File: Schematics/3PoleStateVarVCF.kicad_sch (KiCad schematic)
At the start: 59 parts, among them J1 Conn_01x12, J2 Conn_01x04, J3 Conn_01x06, J4 Conn_01x03, U1 TL074, U2 SSI2164, U3 TL074, U4 TL074

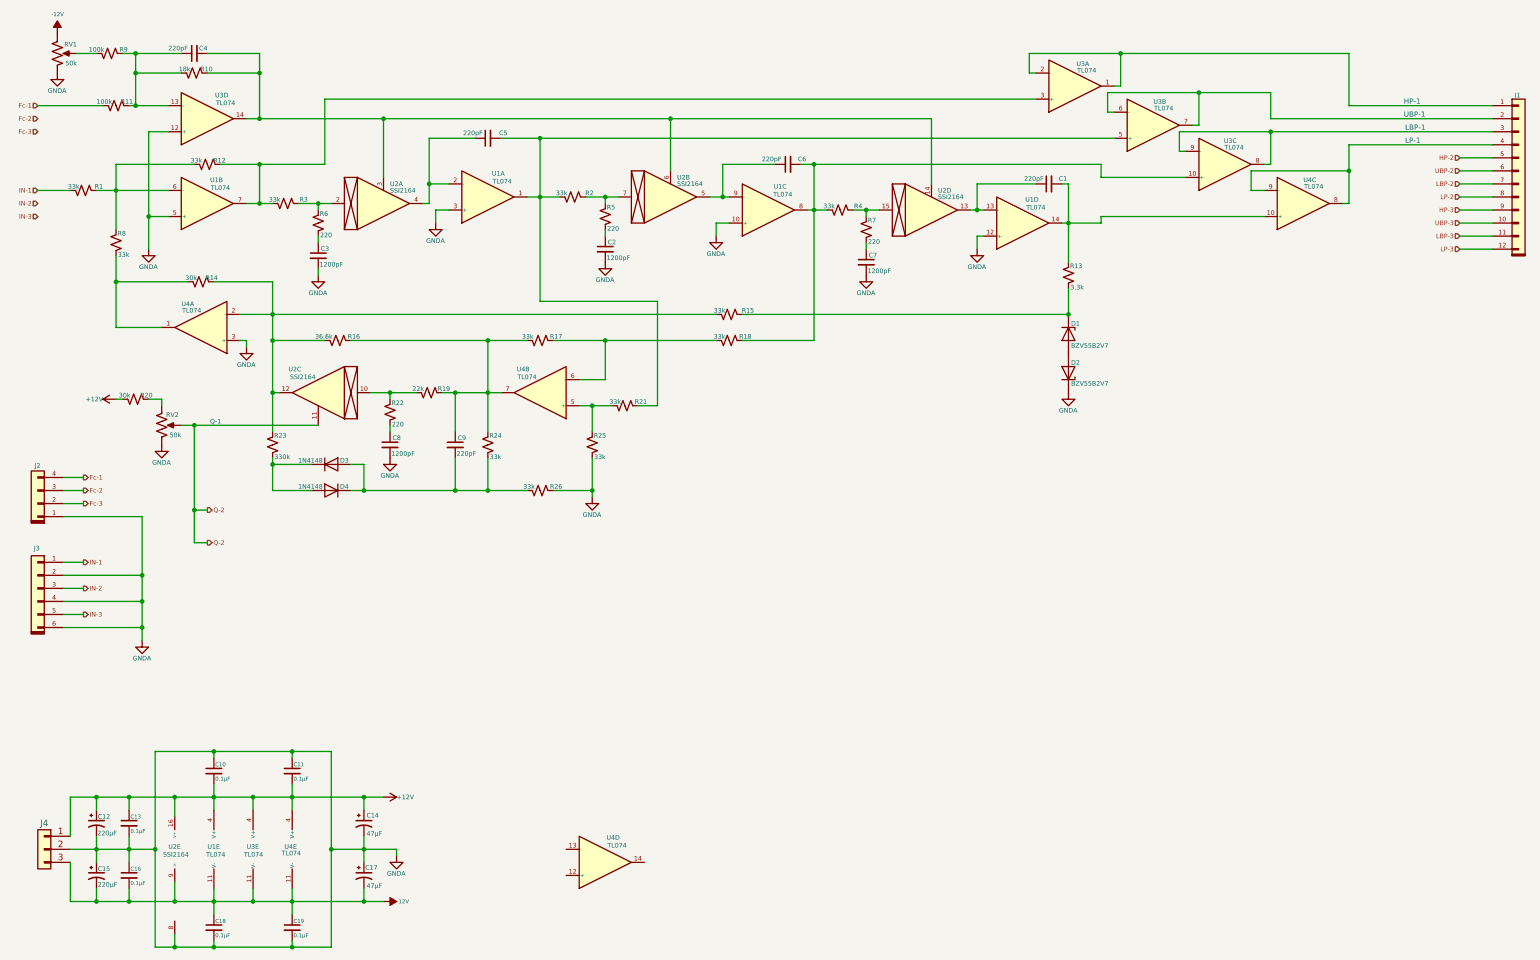
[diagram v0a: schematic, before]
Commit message: Upgreade byte value interface to short.  First stage of refactoring midi input for rotory encoders.  Still needs scaling.
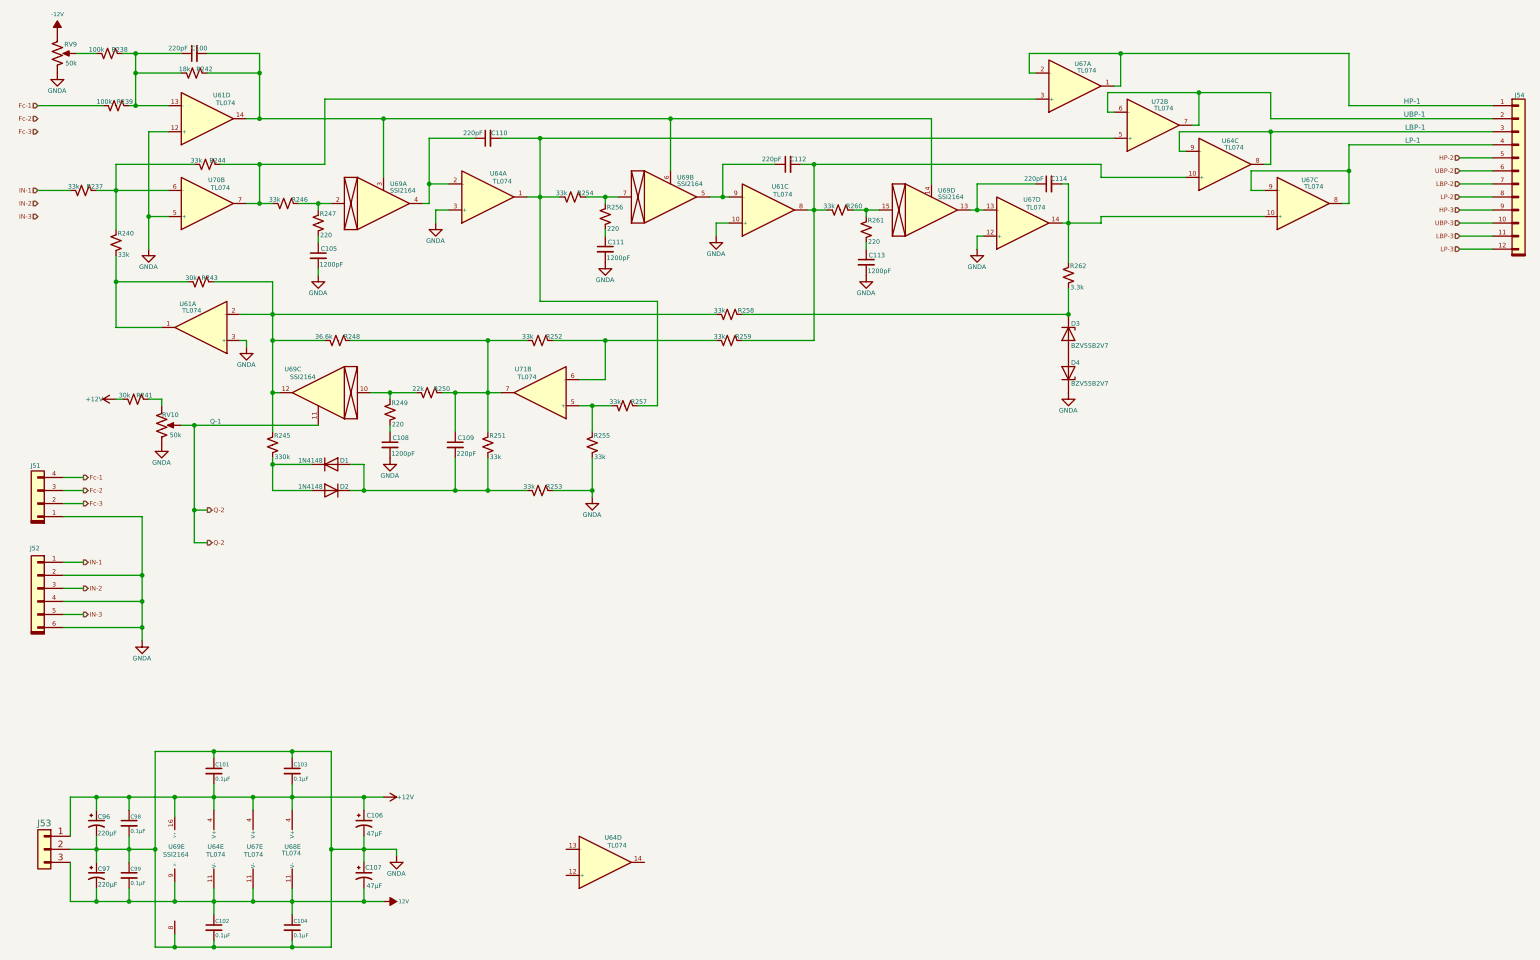
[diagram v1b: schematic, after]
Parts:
- renumbered C4 to C100, C10 to C101, C18 to C102, C11 to C103, C19 to C104, C3 to C105, C14 to C106, C17 to C107, C8 to C108, C9 to C109, C5 to C110, C2 to C111, C6 to C112, C7 to C113, C1 to C114, C12 to C96, C15 to C97, C13 to C98, C16 to C99, D3 to D1, D4 to D2, D1 to D3, D2 to D4, J2 to J51, J3 to J52, J4 to J53, J1 to J54, R1 to R237, R9 to R238, R11 to R239, R8 to R240, R20 to R241, R10 to R242, R14 to R243, R12 to R244, R23 to R245, R3 to R246, R6 to R247, R16 to R248, R22 to R249, R19 to R250, R24 to R251, R17 to R252, R26 to R253, R2 to R254, R25 to R255, R5 to R256, R21 to R257, R15 to R258, R18 to R259, R4 to R260, R7 to R261, R13 to R262, RV2 to RV10, RV1 to RV9, U3 to U61, U1 to U61, U4 to U61, U1 to U64, U4 to U64, U3 to U64, U1 to U67, U3 to U67, U4 to U67, U4 to U68, U2 to U69, U1 to U70, U4 to U71, U3 to U72

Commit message: Updated schematics including VCO and VCF daughter boards
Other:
- title: (none) -> Three State VCF
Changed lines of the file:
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@@
 	(generator_version "8.0")
 	(paper "USLegal")
+	(title_block
+		(title "Three State VCF")
+		(date "2025-01-16")
+		(rev "2.0")
+		(comment 1 "In Development ")
+	)
 	(junction
 		(at 92.71 88.9)

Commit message: Cleaned up page advance on display controls.
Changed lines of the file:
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@@
 (kicad_sch
-	(version 20231120)
+	(version 20250114)
 	(generator "eeschema")
-	(generator_version "8.0")
+	(generator_version "9.0")
 	(paper "USLegal")
 	(title_block
@@
 		(comment 1 "In Development ")
 	)
+	(text "LP-1"
+		(exclude_from_sim no)
+		(at 290.322 40.64 0)
+		(effects
+			(font
+				(size 1.016 1.016)
+			)
+			(justify left bottom)
+		)
+	)
+	(text "UBP-1"
+		(exclude_from_sim no)
+		(at 290.068 35.56 0)
+		(effects
+			(font
+				(size 1.016 1.016)
+			)
+			(justify left bottom)
+		)
+	)
+	(text "LBP-1"
+		(exclude_from_sim no)
+		(at 290.322 38.1 0)
+		(effects
+			(font
+				(size 1.016 1.016)
+			)
+			(justify left bottom)
+		)
+	)
+	(text "HP-1"
+		(exclude_from_sim no)
+		(at 290.068 33.02 0)
+		(effects
+			(font
+				(size 1.016 1.016)
+			)
+			(justify left bottom)
+		)
+	)
+	(text "Q-1"
+		(exclude_from_sim no)
+		(at 57.658 95.25 0)
+		(effects
+			(font
+				(size 0.889 0.889)
+			)
+			(justify left bottom)
+		)
+	)
 	(junction
 		(at 92.71 88.9)
@@
 		)
 	)
-	(text "LP-1"
-		(exclude_from_sim no)
-		(at 290.322 40.64 0)
-		(effects
-			(font
-				(size 1.016 1.016)
-			)
-			(justify left bottom)
-		)
-	)
-	(text "UBP-1"
-		(exclude_from_sim no)
-		(at 290.068 35.56 0)
-		(effects
-			(font
-				(size 1.016 1.016)
-			)
-			(justify left bottom)
-		)
-	)
-	(text "LBP-1"
-		(exclude_from_sim no)
-		(at 290.322 38.1 0)
-		(effects
-			(font
-				(size 1.016 1.016)
-			)
-			(justify left bottom)
-		)
-	)
-	(text "HP-1"
-		(exclude_from_sim no)
-		(at 290.068 33.02 0)
-		(effects
-			(font
-				(size 1.016 1.016)
-			)
-			(justify left bottom)
-		)
-	)
-	(text "Q-1"
-		(exclude_from_sim no)
-		(at 57.658 95.25 0)
-		(effects
-			(font
-				(size 0.889 0.889)
-			)
-			(justify left bottom)
-		)
-	)
 	(hierarchical_label "HP-3"
 		(shape input)
 		(at 300.99 53.34 180)
-		(fields_autoplaced yes)
 		(effects
 			(font
@@
 		(shape output)
 		(at 33.02 105.41 0)
-		(fields_autoplaced yes)
 		(effects
 			(font
@@
 		(shape output)
 		(at 33.02 127 0)
-		(fields_autoplaced yes)
 		(effects
 			(font
@@
 		(shape input)
 		(at 24.13 35.56 180)
-		(fields_autoplaced yes)
 		(effects
 			(font
@@
 		(shape input)
 		(at 24.13 33.02 180)
-		(fields_autoplaced yes)
 		(effects
 			(font
@@
 		(shape input)
 		(at 300.99 58.42 180)
-		(fields_autoplaced yes)
 		(effects
 			(font
@@
 		(shape output)
 		(at 33.02 121.92 0)
-		(fields_autoplaced yes)
 		(effects
 			(font
@@
 		(shape input)
 		(at 24.13 54.61 180)
-		(fields_autoplaced yes)
 		(effects
 			(font
@@
 		(shape input)
 		(at 300.99 43.18 180)
-		(fields_autoplaced yes)
 		(effects
 			(font
@@
 		(shape output)
 		(at 33.02 107.95 0)
-		(fields_autoplaced yes)
 		(effects
 			(font
@@
 		(shape input)
 		(at 24.13 49.53 180)
-		(fields_autoplaced yes)
 		(effects
 			(font
@@
 		(shape input)
 		(at 300.99 50.8 180)
-		(fields_autoplaced yes)
 		(effects
 			(font
@@
 		(shape input)
 		(at 300.99 55.88 180)
-		(fields_autoplaced yes)
 		(effects
 			(font
@@
 		(shape output)
 		(at 33.02 110.49 0)
-		(fields_autoplaced yes)
 		(effects
 			(font
@@
 		(shape output)
 		(at 57.15 118.11 0)
-		(fields_autoplaced yes)
 		(effects
 			(font
@@
 		(shape input)
 		(at 300.99 45.72 180)
-		(fields_autoplaced yes)
 		(effects
 			(font
@@
 		(shape input)
 		(at 24.13 38.1 180)
-		(fields_autoplaced yes)
 		(effects
 			(font
@@
 		(shape output)
 		(at 57.15 111.76 0)
-		(fields_autoplaced yes)
 		(effects
 			(font
@@
 		(shape input)
 		(at 24.13 52.07 180)
-		(fields_autoplaced yes)
 		(effects
 			(font
@@
 		(shape input)
 		(at 300.99 48.26 180)
-		(fields_autoplaced yes)
 		(effects
 			(font
@@
 		(shape input)
 		(at 300.99 60.96 180)
-		(fields_autoplaced yes)
 		(effects
 			(font
@@
 		(shape output)
 		(at 33.02 132.08 0)
-		(fields_autoplaced yes)
 		(effects
 			(font

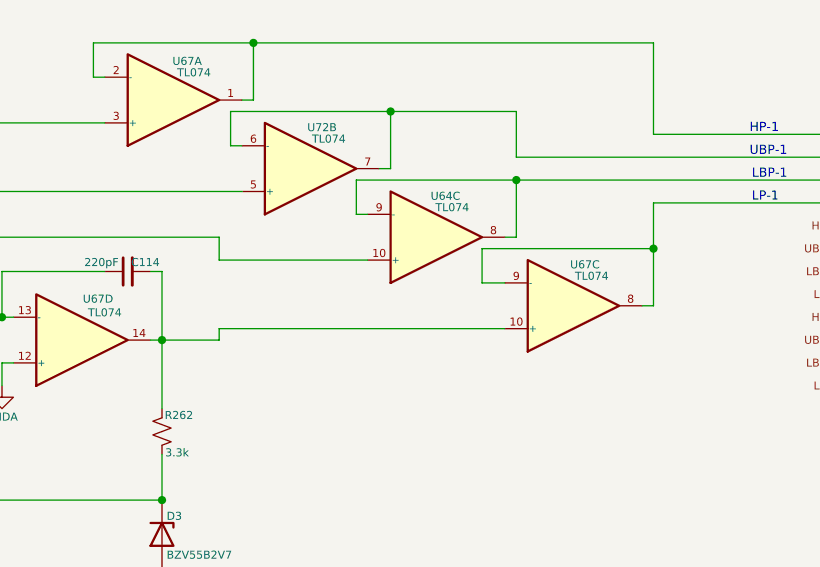
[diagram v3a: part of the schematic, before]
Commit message: minor adjustments for modulation control interface.
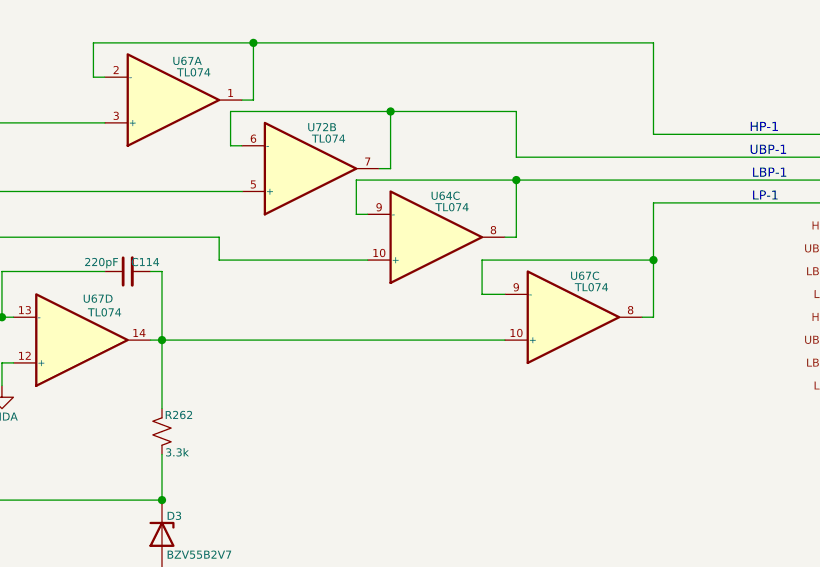
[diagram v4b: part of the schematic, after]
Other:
- moved on the sheet: U67C
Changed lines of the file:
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@@
 	)
 	(junction
-		(at 279.4 45.72)
+		(at 279.4 46.99)
 		(diameter 0)
 		(color 0 0 0 0)
@@
 	(wire
 		(pts
-			(xy 262.89 49.53) (xy 260.35 49.53)
+			(xy 262.89 50.8) (xy 260.35 50.8)
 		)
 		(stroke
@@
 	(wire
 		(pts
-			(xy 231.14 54.61) (xy 262.89 54.61)
-		)
-		(stroke
-			(width 0)
-			(type default)
-		)
-	)
-	(wire
-		(pts
 			(xy 300.99 43.18) (xy 307.34 43.18)
 		)
@@
 	(wire
 		(pts
-			(xy 231.14 55.88) (xy 231.14 54.61)
-		)
-		(stroke
-			(width 0)
-			(type default)
-		)
-	)
-	(wire
-		(pts
 			(xy 232.41 34.29) (xy 233.68 34.29)
 		)
@@
 	(wire
 		(pts
-			(xy 279.4 40.64) (xy 279.4 45.72)
+			(xy 279.4 40.64) (xy 279.4 46.99)
 		)
 		(stroke
@@
 	(wire
 		(pts
-			(xy 279.4 52.07) (xy 278.13 52.07)
+			(xy 279.4 53.34) (xy 278.13 53.34)
 		)
 		(stroke
@@
 	(wire
 		(pts
-			(xy 260.35 45.72) (xy 279.4 45.72)
+			(xy 260.35 46.99) (xy 279.4 46.99)
 		)
 		(stroke
@@
 	(wire
 		(pts
-			(xy 224.79 55.88) (xy 231.14 55.88)
+			(xy 224.79 55.88) (xy 262.89 55.88)
 		)
 		(stroke
@@
 	(wire
 		(pts
-			(xy 279.4 45.72) (xy 279.4 52.07)
+			(xy 279.4 46.99) (xy 279.4 53.34)
 		)
 		(stroke
@@
 	(wire
 		(pts
-			(xy 260.35 49.53) (xy 260.35 45.72)
+			(xy 260.35 50.8) (xy 260.35 46.99)
 		)
 		(stroke
@@
 	(symbol
 		(lib_id "My Chips:TL074")
-		(at 270.51 52.07 0)
+		(at 270.51 53.34 0)
 		(unit 3)
 		(exclude_from_sim no)
@@
 		(dnp no)
 		(property "Reference" "U67"
-			(at 271.78 47.498 0)
+			(at 271.78 48.768 0)
 			(effects
 				(font
@@
 		)
 		(property "Value" "TL074"
-			(at 272.542 48.768 0)
+			(at 272.542 50.038 0)
 			(effects
 				(font
@@
 		)
 		(property "Footprint" ""
-			(at 269.24 49.53 0)
+			(at 269.24 50.8 0)
 			(effects
 				(font
@@
 		)
 		(property "Datasheet" "http://www.ti.com/lit/ds/symlink/lm2902-n.pdf"
-			(at 271.78 44.45 0)
+			(at 271.78 45.72 0)
 			(effects
 				(font
@@
 		)
 		(property "Description" ""
-			(at 270.51 52.07 0)
+			(at 270.51 53.34 0)
 			(effects
 				(font

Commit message: Fixed bugs in voice selection on configuration.  Reorganized schematics to have different master drawings for power and audio paths.  Started work on dual 3-pole state variable filter with resonance.
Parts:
- removed C98, C99: 0.1µF, symbol Device:C_Small
- removed J52: Conn_01x06, symbol My Connectors:Conn_01x06
- removed J54: Conn_01x12, symbol My Connectors:Conn_01x12
- removed U61, U64, U67, U68, U70, U71, U72: TL074, symbol My Chips:TL074
- added C421, C432, C438, C442, C80, C81, C82, C83, C84, C85, C86, C87, C88, C89: 0.1µF, symbol Device:C_Small
- added C71, C74, C75, C77, C79: 220pF, symbol Device:C_Small
- added C72, C73, C76, C78: 1200pF, symbol Device:C_Small
- added D20, D21: 1N4148, Diode_SMD:D_SOD-123, symbol Diode:1N4148W
- added D22, D23: BZV55B2V7, Diode_SMD:D_MiniMELF, symbol Diode:BZV55B2V7
- added R56, R59, R63, R65, R70, R71, R72, R73, R74, R76, R77, R78, R79, R82, R83, R84, R85, R86, R87, R88, R89: 33k, symbol Device:R_Small_US
- added R57, R58: 100k, symbol Device:R_Small_US
- added R60, R62: 30k, symbol Device:R_Small_US
- added R61: 18k, symbol Device:R_Small_US
- added R64: 330k, symbol Device:R_Small_US
- added R66, R68, R75, R80: 220, symbol Device:R_Small_US
- added R67: 36.6k, symbol Device:R_Small_US
- added R69: 22k, symbol Device:R_Small_US
- added R81: 3.3k, symbol Device:R_Small_US
- added RV8, RV9: 50k, symbol Device:R_Potentiometer_US
- added U270, U277: DG212C, symbol My Chips:DG212C
- added U33, U37, U42, U43: TL072, symbol Amplifier_Operational:TL072
- added U34, U36, U38 (x2): TL074, symbol Amplifier_Operational:TL074
- added U35: TL074, symbol My Chips:TL074
- added U39: SSI2164, symbol SSI2164:SSI2164
- renumbered C96 to C51, C97 to C52, C100 to C55, C101 to C56, C102 to C57, C103 to C58, C104 to C59, C105 to C60, C108 to C61, C106 to C62, C107 to C63, C109 to C64, C110 to C65, C111 to C66, C112 to C67, C113 to C68, C114 to C70, D1 to D16, D2 to D17, D3 to D18, D4 to D19, J51 to J54, J53 to J55, R238 to R27, R239 to R28, R237 to R32, R240 to R33, R241 to R34, R242 to R35, R243 to R36, R244 to R37, R245 to R38, R246 to R39, R247 to R40, R248 to R41, R249 to R42, R250 to R43, R251 to R44, R252 to R45, R253 to R46, R254 to R47, R255 to R48, R256 to R49, R257 to R50, R258 to R51, R259 to R52, R260 to R53, R261 to R54, R262 to R55, RV9 to RV6, RV10 to RV7, U69 to U32
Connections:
- net Fc-3 is gone; now on net IN-1: J54.2 (Pin_2)
- net +12V: now also C432.2, C442.2, C80.2, C81.2, C84.2, C85.2, C86.2, R60.2, U270.13 (V+), U277.13 (V+), U33.8 (V+), U34.4 (V+), U35.4 (V+), U36.4 (V+), U37.8 (V+), U38.4 (V+), U39.16 (V+), U42.8 (V+)
- net -12V: now also C421.1, C438.1, C82.1, C83.1, C87.1, C88.1, C89.1, RV8. (2), U270.4 (V-), U277.4 (V-), U33.4 (V-), U34.11 (V-), U35.11 (V-), U36.11 (V-), U37.4 (V-), U38.11 (V-), U39.9 (V-), U42.4 (V-)
- net Fc-1: no longer J54.4 (Pin_4)
- net Fc-2: now also R57.2; no longer J54.3 (Pin_3)
- net GNDA: now also C72.2, C73.2, C76.2, C78.2, C80.1, C81.1, C82.2, C83.2, C84.1, C85.1, C86.1, C87.2, C88.2, C89.2, D23.1 (K), R72.1, R74.2, RV8. (2), RV9. (2), U33.3 (+), U33.5 (+), U34.10 (+), U34.3 (+), U34.5 (+), U36.10 (+), U36.3 (+), U36.5 (+), U39.8, U42.3 (+), U42.5 (+), U43.3 (+), U43.5 (+); no longer J54.1 (Pin_1)
- net IN-2: now also J54.4 (Pin_4), R56.2
- net at C64.1, R41.1, R43.1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: now also U34.14
- net at C55.1, R27.1, R28.1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: now also U42.2 (-)
- net at C55.2, R35.1, U32.3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: now also U32.11, U42.1; no longer U32.14
- net at C67.2, R52.1, R53.2: now also U34.7, U35.9 (-)
- net at C67.1, U32.5: now also U34.6 (-)
- net at R53.1, R54.1: now also U32.10; no longer U32.15
- net at C70.2, R55.1: now also U34.8, U35.12 (+)
- net at U32.13: now also R36.1, R38.1, R41.2, R51.2, U33.6 (-); no longer C70.1
- net at C65.1, U32.4: now also U34.2 (-)
- net at R42.1, R43.2: now also U32.15; no longer U32.10
- net at R48.1, R50.2: now also U34.12 (+)
- net at R32.1, R33.1, R37.2: now also U33.2 (-)
- net at R33.2, R36.2: now also U33.7
- net at C65.2, R47.2, R50.1: now also U34.1, U35.6 (-)
- net at R45.1, R52.2: now also U34.13 (-)
- net at R37.1, R39.2: now also U33.1, U35.2 (-)
- removed net Q-2: RV7. (2), U32.11
- new net: R73.1, R75.1, U39.7
- new net: C76.1, R75.2
- new net: D20.1 (K), D21.2 (A), R64.2
- new net: C74.2, D20.2 (A), D21.1 (K), R70.2, R72.2
- new net: R63.1, R65.2, U38.3 (+), U43.1
- new net: R56.1, R59.1, R63.2, U43.2 (-)
- new net: C421.2, C432.1, U270.5 (GND)
- new net: R82.1, R83.1, R84.1, R85.1
- new net: R84.2, U270.10 (D3)
- new net: C75.2, R73.2, R76.1, U36.1, U38.5 (+)
- new net: C75.1, U36.2 (-), U39.4
- new net: C77.2, R78.1, R79.2, U36.7, U38.10 (+)
- new net: R71.1, R78.2, U36.13 (-)
- new net: R79.1, R80.1, U39.10
- new net: C71.2, R61.1, U39.11, U39.3, U39.6, U42.7
- new net: C79.1, U36.9 (-), U39.12
- new net: U270.14 (S2), U35.5 (+), U35.7
- new net: U270.11 (S3), U35.10 (+), U35.8
- new net: R83.2, U270.15 (D2)
- new net: R82.2, U270.2 (D1)
- new net: U270.3 (S1), U35.1, U35.3 (+)
- new net: U270.6 (S4), U35.13 (-), U35.14
- new net: R85.2, U270.7 (D4)
- new net: C77.1, U36.6 (-), U39.5
- new net: R86.1, R87.1, R88.1, R89.1
- new net: R88.2, U277.10 (D3)
- new net: C79.2, R81.1, U36.8, U38.12 (+)
- new net: R87.2, U277.15 (D2)
- new net: R68.1, R69.2, U39.15
- new net: C73.1, R68.2
- new net: U277.11 (S3), U38.8, U38.9 (-)
- new net: U277.14 (S2), U277.3 (S1), U38.1, U38.2 (-), U38.6 (-), U38.7
- new net: R86.2, U277.2 (D1)
- new net: C438.2, C442.1, U277.5 (GND)
- new net: U277.6 (S4), U38.13 (-), U38.14
- new net: R89.2, U277.7 (D4)
- new net: C78.1, R80.2
- new net: R65.1, R66.1, U39.2
- new net: C72.1, R66.2
- new net: D22.1 (K), R77.1, R81.2
- new net: D22.2 (A), D23.2 (A)
- new net: RV7. (2), U32.14
- new net: R58.2, RV8. (2)
- new net: C70.1, U32.12, U34.9 (-)
- new net: C71.1, R57.1, R58.1, R61.2, U42.6 (-)
- new net: R62.1, R64.1, R67.2, R77.2, U39.13, U43.6 (-)
- new net: RV9. (2), U39.14
- new net: R59.2, R62.2, U43.7
- new net: R60.1, RV9. (2)
- new net: C74.1, R67.1, R69.1, R70.1, R71.2, U36.14
- new net: R74.1, R76.2, U36.12 (+)
- new net +3.3V: U270.12 (VL), U277.12 (VL)
- new net S0: U270.1 (IN1), U277.1 (IN1)
- new net S1: U270.16 (IN2), U277.16 (IN2)
- new net S2: U270.9 (IN3), U277.9 (IN3)
- new net S3: U270.8 (IN4), U277.8 (IN4)
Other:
- note added: "HP-2"
- note added: "LBP-2"
- note added: "LP-2"
- note added: "UBP-2"
- moved on the sheet: C51, C52, C55, C56, C57, C58, C59, C60, C61, C62, C63, C64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
